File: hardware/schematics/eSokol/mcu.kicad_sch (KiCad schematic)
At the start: 15 parts, among them J1 DB25, Q6 AO3400A, SW1 SW_LITTLE, U2 YAAJ_BluePill_SWD_Breakout, U3 TP4056, U5 AMS1117-5.0, U9 TCRT5000

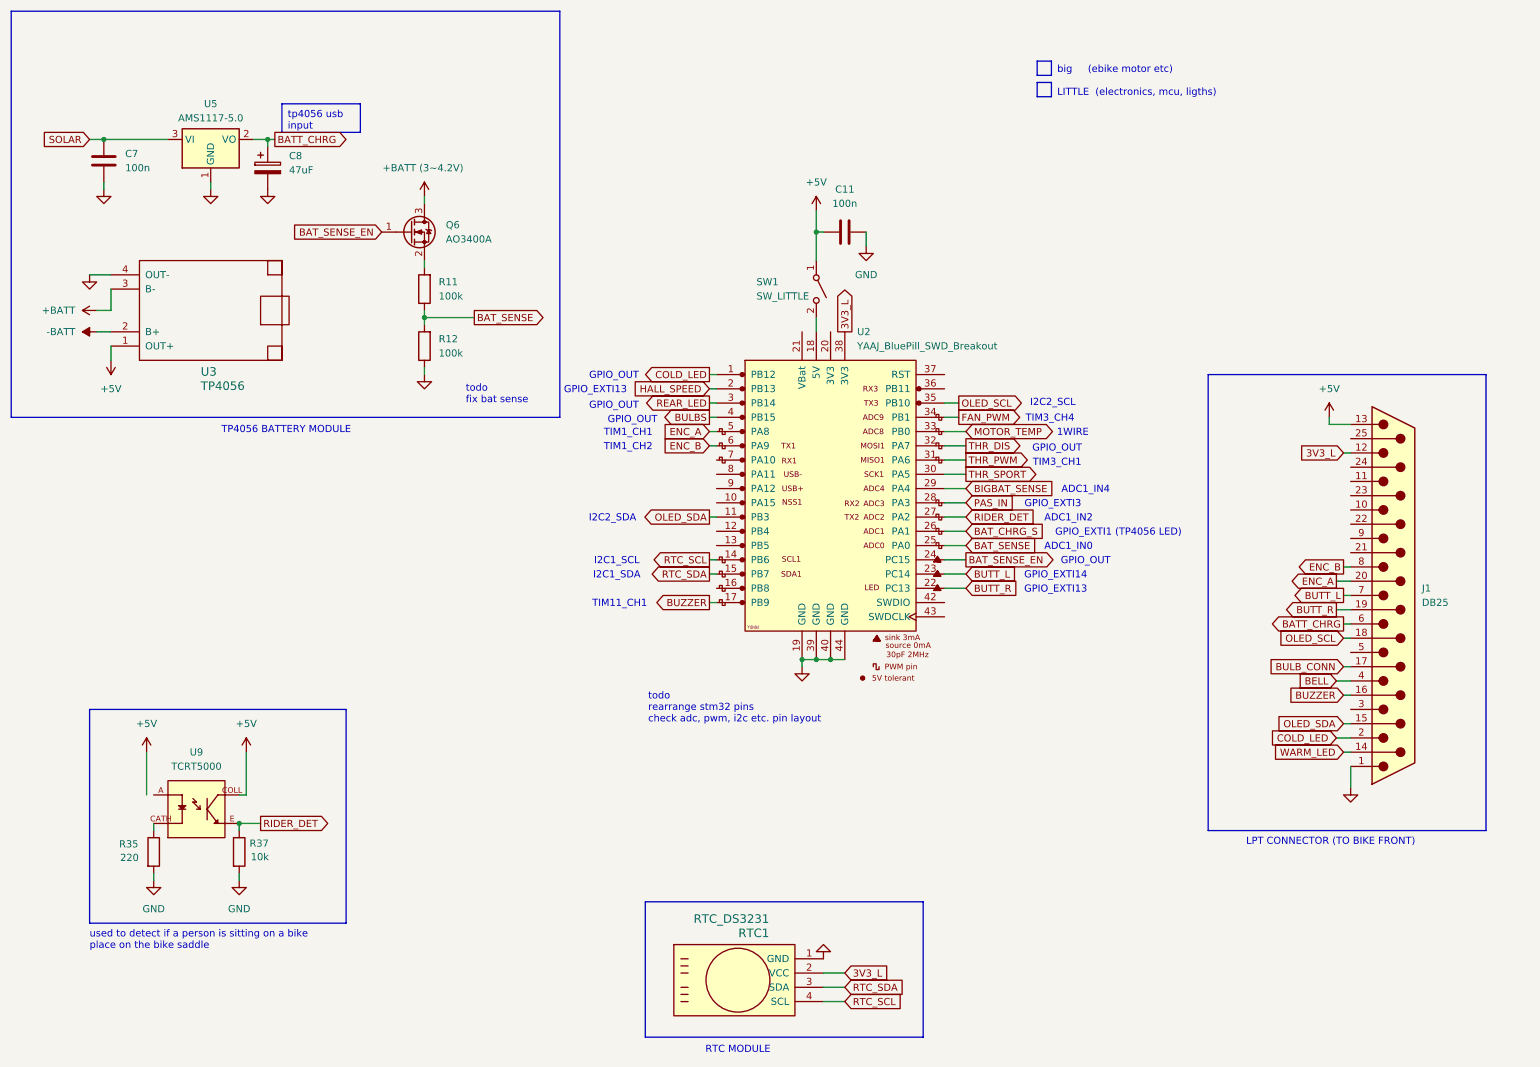
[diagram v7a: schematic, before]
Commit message: hardware/schematics: Replace screen-based control for HC-05 smartphone-app-based control, add buzzer RC filter, rework cold LED circuit
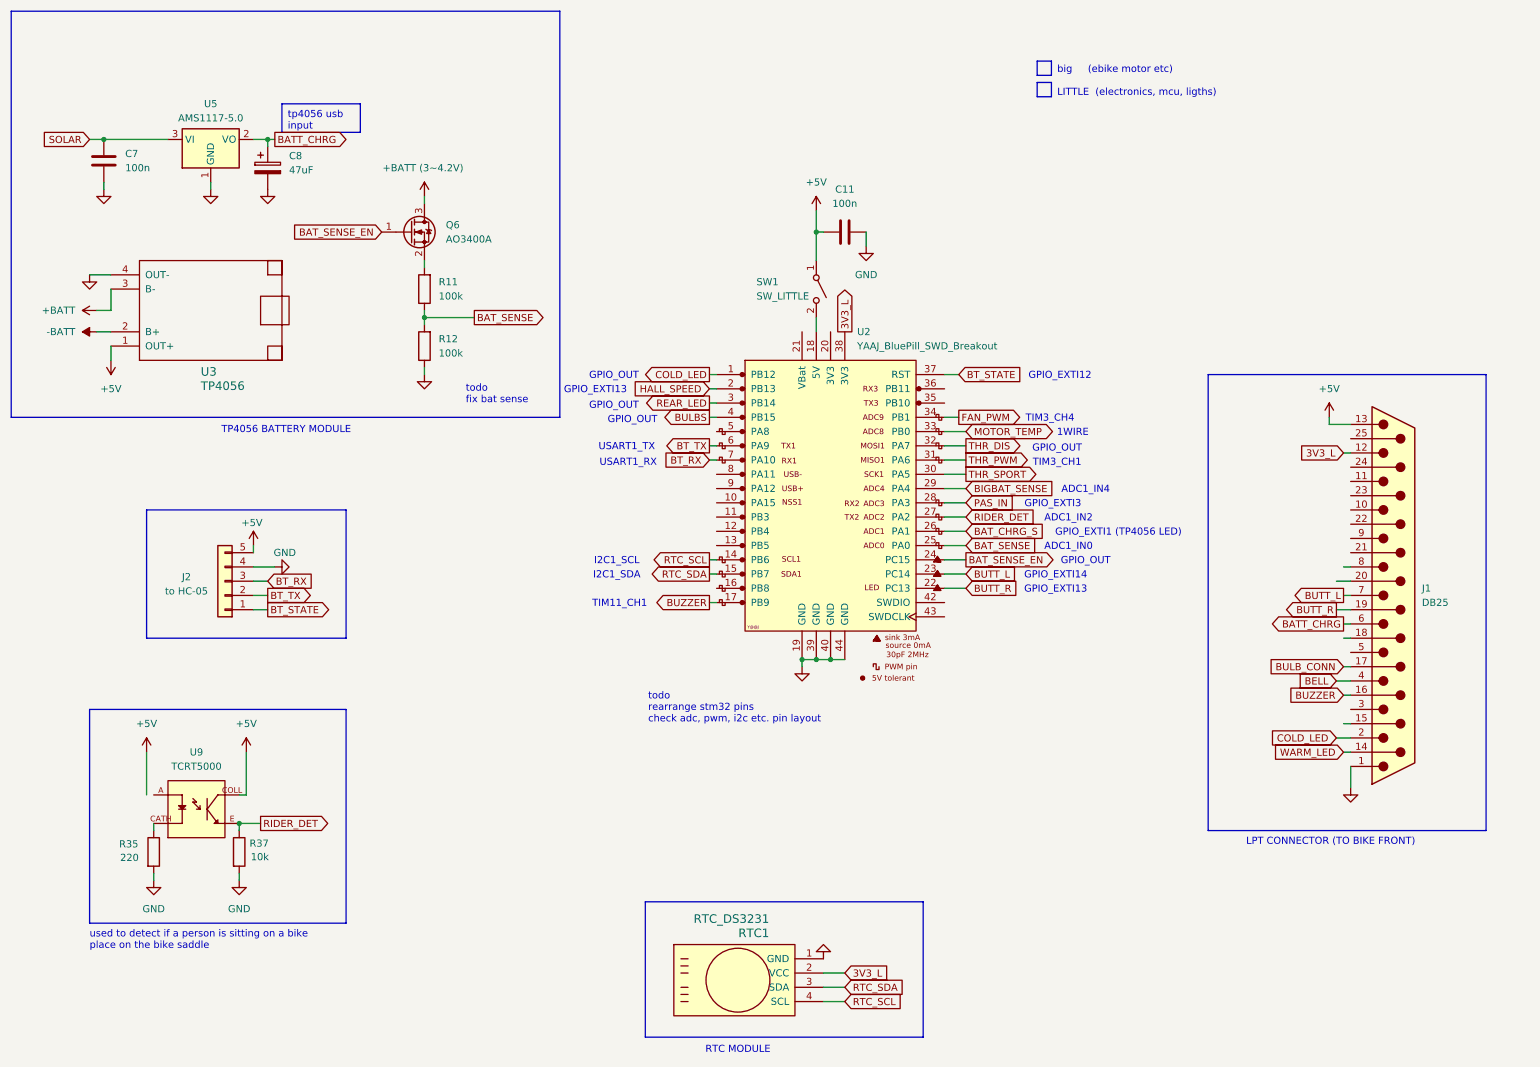
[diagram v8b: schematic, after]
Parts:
- added J2: to HC-05, symbol Connector_Generic:Conn_01x05
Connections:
- net +5V: now also J2.5 (Pin_5)
- net GND: now also J2.4 (Pin_4)
- net BT_STATE: now reaches U2.37 (RST)
- net BT_STATE: now also J2.1 (Pin_1)
- net BT_RX: now reaches U2.7 (PA10)
- net BT_RX: now also J2.3 (Pin_3)
- net ENC_A: no longer names the net of J1.20 (P20)
- net ENC_A: no longer U2.5 (PA8)
- net ENC_B: no longer names the net of J1.8
- net ENC_B: no longer U2.6 (PA9)
- net OLED_SCL: no longer names the net of J1.18 (P18)
- net OLED_SCL: no longer U2.35 (PB10)
- net OLED_SDA: no longer names the net of J1.15 (P15)
- net OLED_SDA: no longer U2.11 (PB3)
- new net BT_TX: J2.2 (Pin_2), U2.6 (PA9)
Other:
- note added: "GPIO_EXTI12"
- note added: "USART1_RX"
- note added: "USART1_TX"
- note removed: "I2C2_SCL"
- note removed: "I2C2_SDA"
- note removed: "TIM1_CH1"
- note removed: "TIM1_CH2"
